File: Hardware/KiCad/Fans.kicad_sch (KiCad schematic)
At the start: 21 parts, among them J7 Conn_01x06, Q1 PSMN8R5-40MSDX, Q5 PSMN8R5-40MSDX

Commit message: revB
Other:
- moved on the sheet: D5, D7, J7, LVPWR16, LVPWR17, LVPWR3, LVPWR6, PWM_A2, PWM_B2, Q1, Q5, R10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

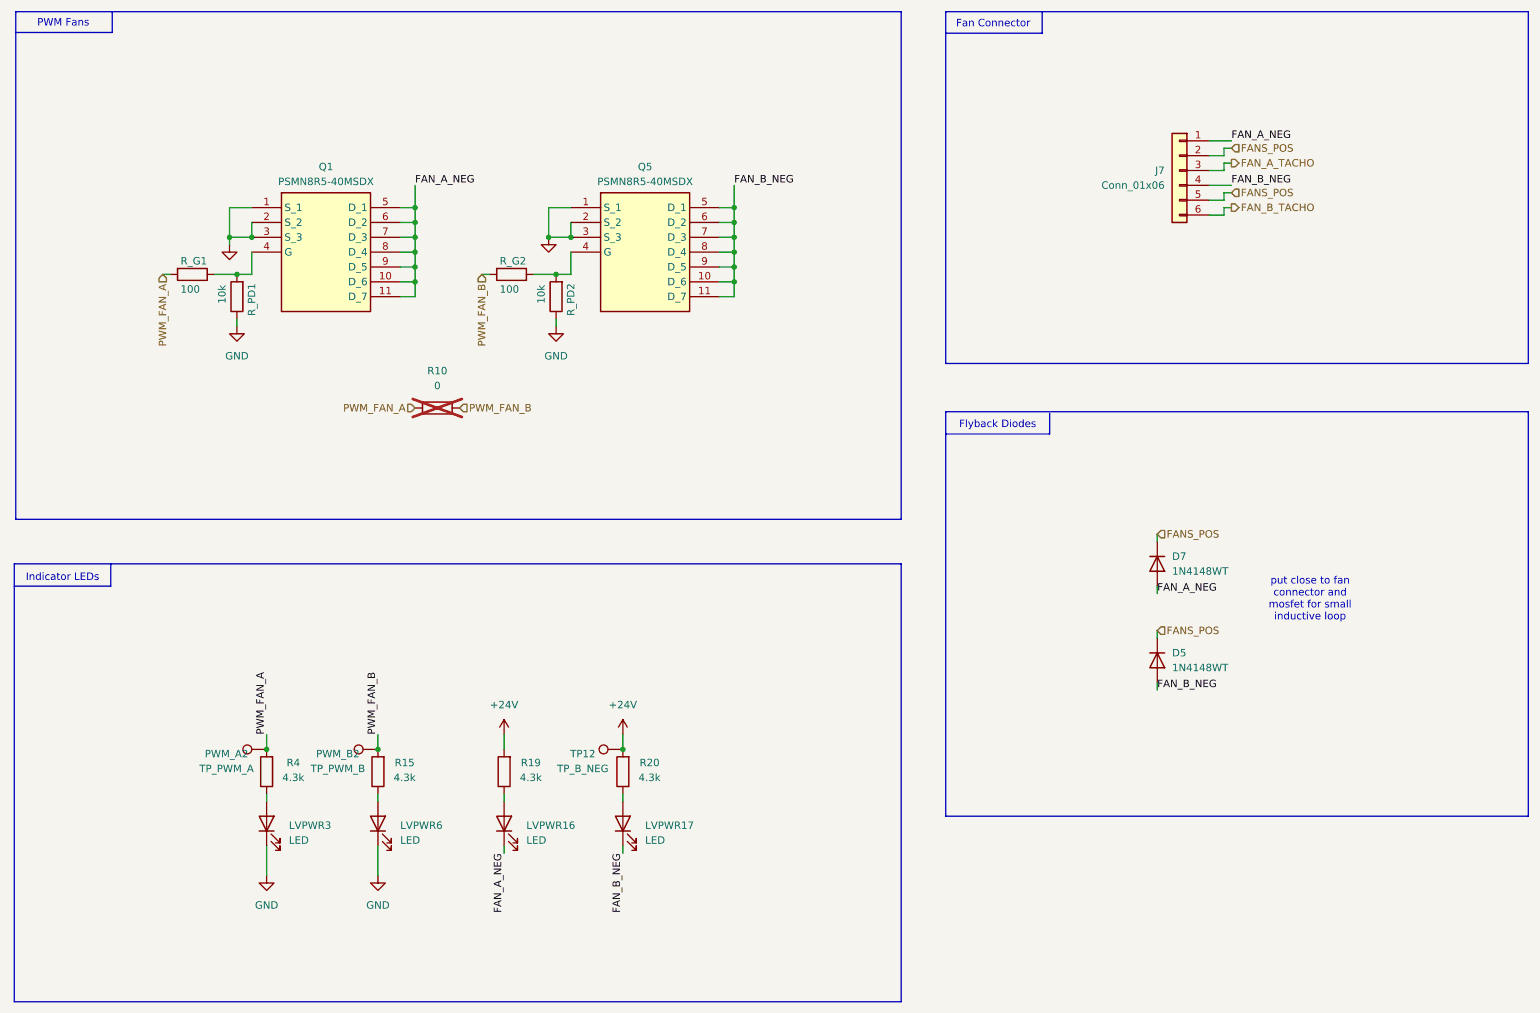
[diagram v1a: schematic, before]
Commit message: schematic changes, pre pcb revB changes
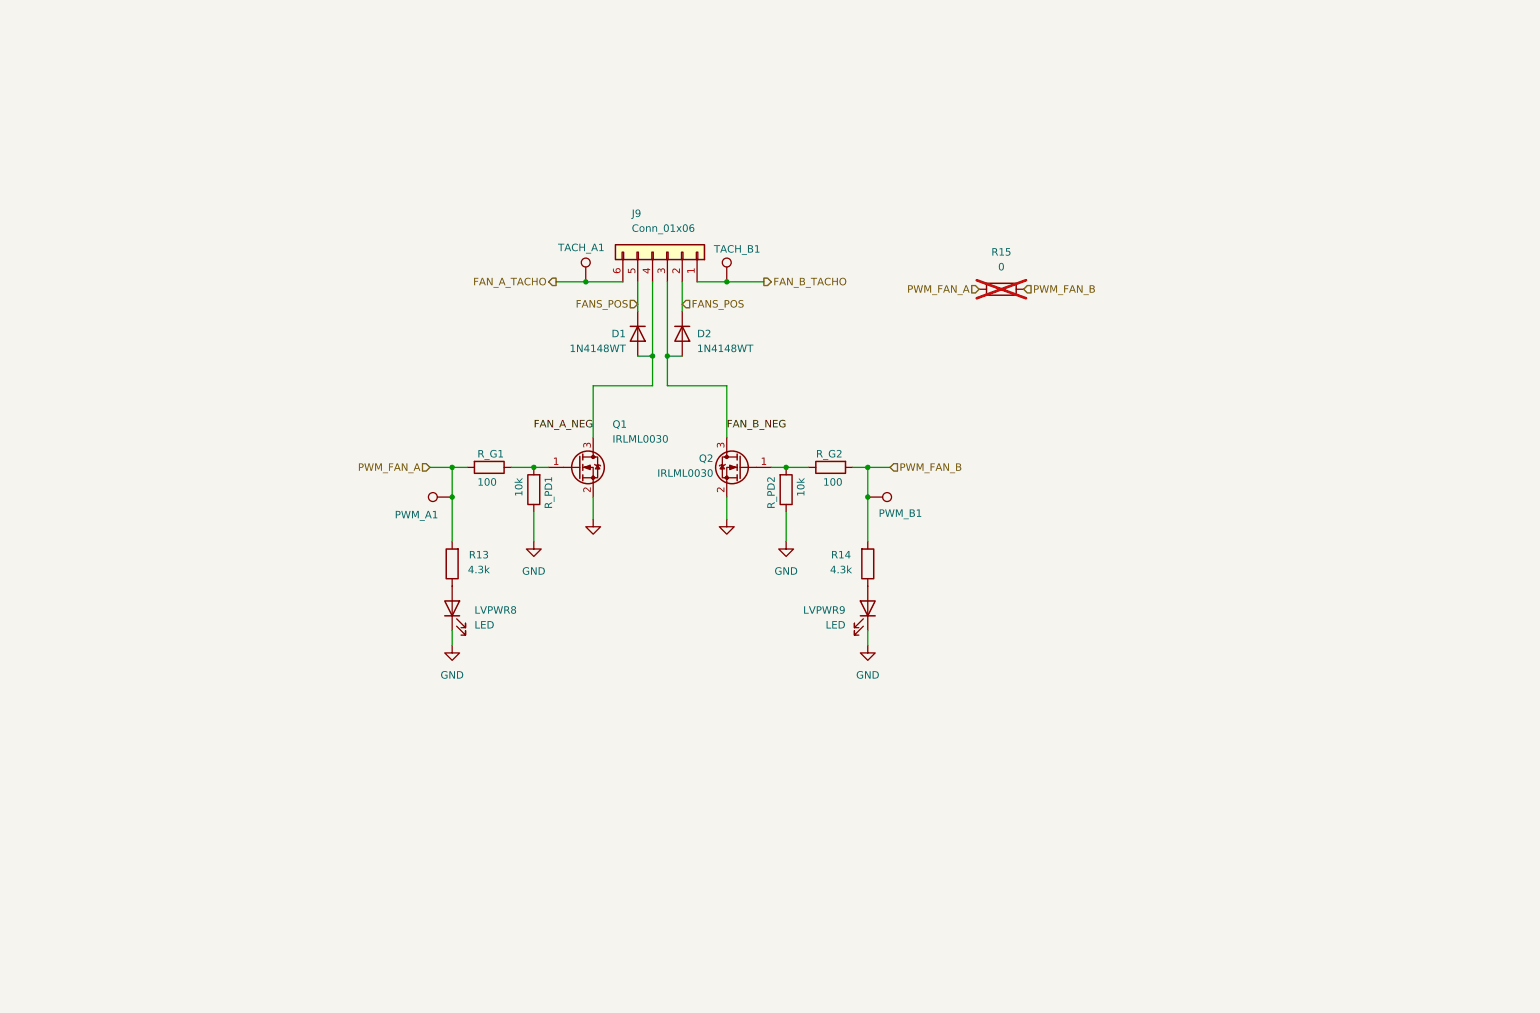
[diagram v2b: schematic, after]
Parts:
- removed LVPWR16, LVPWR17: LED, LED_SMD:LED_0603_1608Metric, symbol Device:LED
- removed Q1, Q5: PSMN8R5-40MSDX, UTSVT_Power:PSMN8R5-40MSDX, symbol UTSVT_Power:PSMN8R5-40MSDX
- removed R19, R20: 4.3k, Resistor_SMD:R_0603_1608Metric_Pad0.98x0.95mm_HandSolder, symbol Device:R
- removed TP12: TP_B_NEG, TestPoint:TestPoint_Pad_1.0x1.0mm, symbol Connector:TestPoint
- added Q1, Q2: IRLML0030, Package_TO_SOT_SMD:SOT-23, symbol Transistor_FET:IRLML0030
- added TACH_A1, TACH_B1: TP_PWM_B, TestPoint:TestPoint_Pad_1.0x1.0mm, symbol Connector:TestPoint
- D1: renamed from D7; footprint Diode_SMD:D_SOD-523 -> easyeda2kicad:SOD-523F_L1.2-W0.8-LS1.7-RD; LCSC (none) -> C27748
- D2: renamed from D5; footprint Diode_SMD:D_SOD-523 -> easyeda2kicad:SOD-523F_L1.2-W0.8-LS1.7-RD; LCSC (none) -> C27748
- R13: renamed from R4; LCSC (none) -> C2907165
- R14: renamed from R15; LCSC (none) -> C2907165
- R15: renamed from R10; LCSC (none) -> C21189
- R_PD1, R_PD2: LCSC (none) -> C25804
- renumbered J7 to J9, LVPWR3 to LVPWR8, LVPWR6 to LVPWR9, PWM_A2 to PWM_A1, PWM_B2 to PWM_B1
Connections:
- net FAN_A_NEG: now also J9.4 (Pin_4), Q1.3 (D); no longer J9.1 (Pin_1)
- net FAN_A_TACHO: now also J9.6 (Pin_6), TACH_A1.1; no longer J9.3 (Pin_3)
- net FAN_B_NEG: now also J9.3 (Pin_3), Q2.3 (D); no longer J9.4 (Pin_4)
- net FAN_B_TACHO: now also J9.1 (Pin_1), TACH_B1.1; no longer J9.6 (Pin_6)
- net GND: now also Q1.2 (S), Q2.2 (S)
- net at R_G2.1, R_PD2.2: now also Q2.1 (G)
- net at R_G1.1, R_PD1.2: now also Q1.1 (G)
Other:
- note removed: "Fan Connector"
- note removed: "Flyback Diodes"
- note removed: "Indicator LEDs"
- note removed: "PWM Fans"
- note removed: "put close to fan connector and mosfet for small inductive loop"
- moved on the sheet: D1, D2, J9, LVPWR8, LVPWR9, PWM_A1, PWM_B1, R13, R14, R15, R_G1, R_PD1

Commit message: revB, will make aesthetic changes
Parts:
- J9: footprint Connector_Molex:Molex_Nano-Fit_105309-xx06_1x06_P2.50mm_Vertical -> Connector_Molex:Molex_Nano-Fit_105313-xx06_1x06_P2.50mm_Horizontal
- renumbered PWM_B1 to PWM_A1, PWM_A1 to PWM_B1, TACH_B1 to TACH_A1, TACH_A1 to TACH_B1
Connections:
- net FAN_A_TACHO: now also J9.1 (Pin_1), TACH_A1.1; no longer J9.6 (Pin_6), TACH_B1.1
- net FAN_B_TACHO: now also J9.6 (Pin_6), TACH_B1.1; no longer J9.1 (Pin_1), TACH_A1.1
- net PWM_FAN_A: now also PWM_A1.1, R14.2, R_G2.2; no longer PWM_B1.1, R13.2, R_G1.2
- net PWM_FAN_B: now also PWM_B1.1, R13.2, R_G1.2; no longer PWM_A1.1, R14.2, R_G2.2
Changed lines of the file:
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@@
 	(wire
 		(pts
-			(xy 139.7 66.04) (xy 146.05 66.04)
+			(xy 139.7 66.04) (xy 144.78 66.04)
 		)
 		(stroke
@@
 	(hierarchical_label "PWM_FAN_B"
 		(shape input)
-		(at 167.64 97.79 0)
+		(at 88.9 97.79 180)
 		(effects
 			(font
 				(size 1.27 1.27)
 			)
-			(justify left)
+			(justify right)
 		)
 	)
 	(hierarchical_label "FAN_A_TACHO"
 		(shape output)
-		(at 110.49 66.04 180)
+		(at 144.78 66.04 0)
 		(effects
 			(font
 				(size 1.27 1.27)
 			)
-			(justify right)
+			(justify left)
 		)
 	)
@@
 	(hierarchical_label "PWM_FAN_A"
 		(shape input)
-		(at 88.9 97.79 180)
+		(at 167.64 97.79 0)
 		(effects
 			(font
 				(size 1.27 1.27)
 			)
-			(justify right)
+			(justify left)
 		)
 	)
 	(hierarchical_label "FAN_B_TACHO"
 		(shape output)
-		(at 146.05 66.04 0)
+		(at 110.49 66.04 180)
 		(effects
 			(font
 				(size 1.27 1.27)
 			)
-			(justify left)
+			(justify right)
 		)
 	)
@@
 		(on_board yes)
 		(dnp no)
-		(property "Reference" "PWM_A1"
+		(property "Reference" "PWM_B1"
 			(at 86.614 105.918 90)
 			(effects
@@
 			(project ""
 				(path "/a2e13c19-ff3a-4e43-a7f5-200fd5b2b978/26b9ca43-4422-48e7-9562-1bb32842f27e"
-					(reference "PWM_A1")
+					(reference "PWM_B1")
 					(unit 1)
 				)
@@
 		(on_board yes)
 		(dnp no)
-		(property "Reference" "TACH_A1"
+		(property "Reference" "TACH_B1"
 			(at 114.808 60.198 0)
 			(effects
@@
 			(project "PS-MotorControllerInterfacePCB"
 				(path "/a2e13c19-ff3a-4e43-a7f5-200fd5b2b978/26b9ca43-4422-48e7-9562-1bb32842f27e"
-					(reference "TACH_A1")
+					(reference "TACH_B1")
 					(unit 1)
 				)
@@
 			)
 		)
-		(property "Footprint" "Connector_Molex:Molex_Nano-Fit_105309-xx06_1x06_P2.50mm_Vertical"
+		(property "Footprint" "Connector_Molex:Molex_Nano-Fit_105313-xx06_1x06_P2.50mm_Horizontal"
 			(at 129.54 60.96 0)
 			(effects
@@
 		(on_board yes)
 		(dnp no)
-		(property "Reference" "PWM_B1"
+		(property "Reference" "PWM_A1"
 			(at 169.418 105.664 90)
 			(effects
@@
 			(project "PS-MotorControllerInterfacePCB"
 				(path "/a2e13c19-ff3a-4e43-a7f5-200fd5b2b978/26b9ca43-4422-48e7-9562-1bb32842f27e"
-					(reference "PWM_B1")
+					(reference "PWM_A1")
 					(unit 1)
 				)
@@
 		(on_board yes)
 		(dnp no)
-		(property "Reference" "TACH_B1"
+		(property "Reference" "TACH_A1"
 			(at 141.478 60.452 0)
 			(effects
@@
 			(project "PS-MotorControllerInterfacePCB"
 				(path "/a2e13c19-ff3a-4e43-a7f5-200fd5b2b978/26b9ca43-4422-48e7-9562-1bb32842f27e"
-					(reference "TACH_B1")
+					(reference "TACH_A1")
 					(unit 1)
 				)

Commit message: revB layout
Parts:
- removed LVPWR8, LVPWR9: LED, LED_SMD:LED_0603_1608Metric, symbol Device:LED
- removed R13, R14: 4.3k, Resistor_SMD:R_0603_1608Metric_Pad0.98x0.95mm_HandSolder, symbol Device:R
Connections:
- net FAN_A_NEG: now also D2.2 (A), Q2.3 (D); no longer D1.2 (A), Q1.3 (D)
- net FAN_B_NEG: now also D1.2 (A), Q1.3 (D); no longer D2.2 (A), Q2.3 (D)
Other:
- moved on the sheet: PWM_A1, PWM_B1

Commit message: sch changes, pre pcb changes
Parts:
- added PD_TACHA1, PD_TACHB1: 10k, Resistor_SMD:R_0603_1608Metric_Pad0.98x0.95mm_HandSolder, symbol Device:R
- D1, D2: footprint easyeda2kicad:SOD-523F_L1.2-W0.8-LS1.7-RD -> Diode_SMD:D_SOD-523
- J9: footprint Connector_Molex:Molex_Nano-Fit_105313-xx06_1x06_P2.50mm_Horizontal -> UTSVT_Connectors:105313-1106
- renumbered R15 to R11
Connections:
- net FAN_A_TACHO: now also PD_TACHA1.1
- net FAN_B_TACHO: now also PD_TACHB1.1
- new net +3V3: PD_TACHA1.2, PD_TACHB1.2
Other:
- moved on the sheet: D1, R11

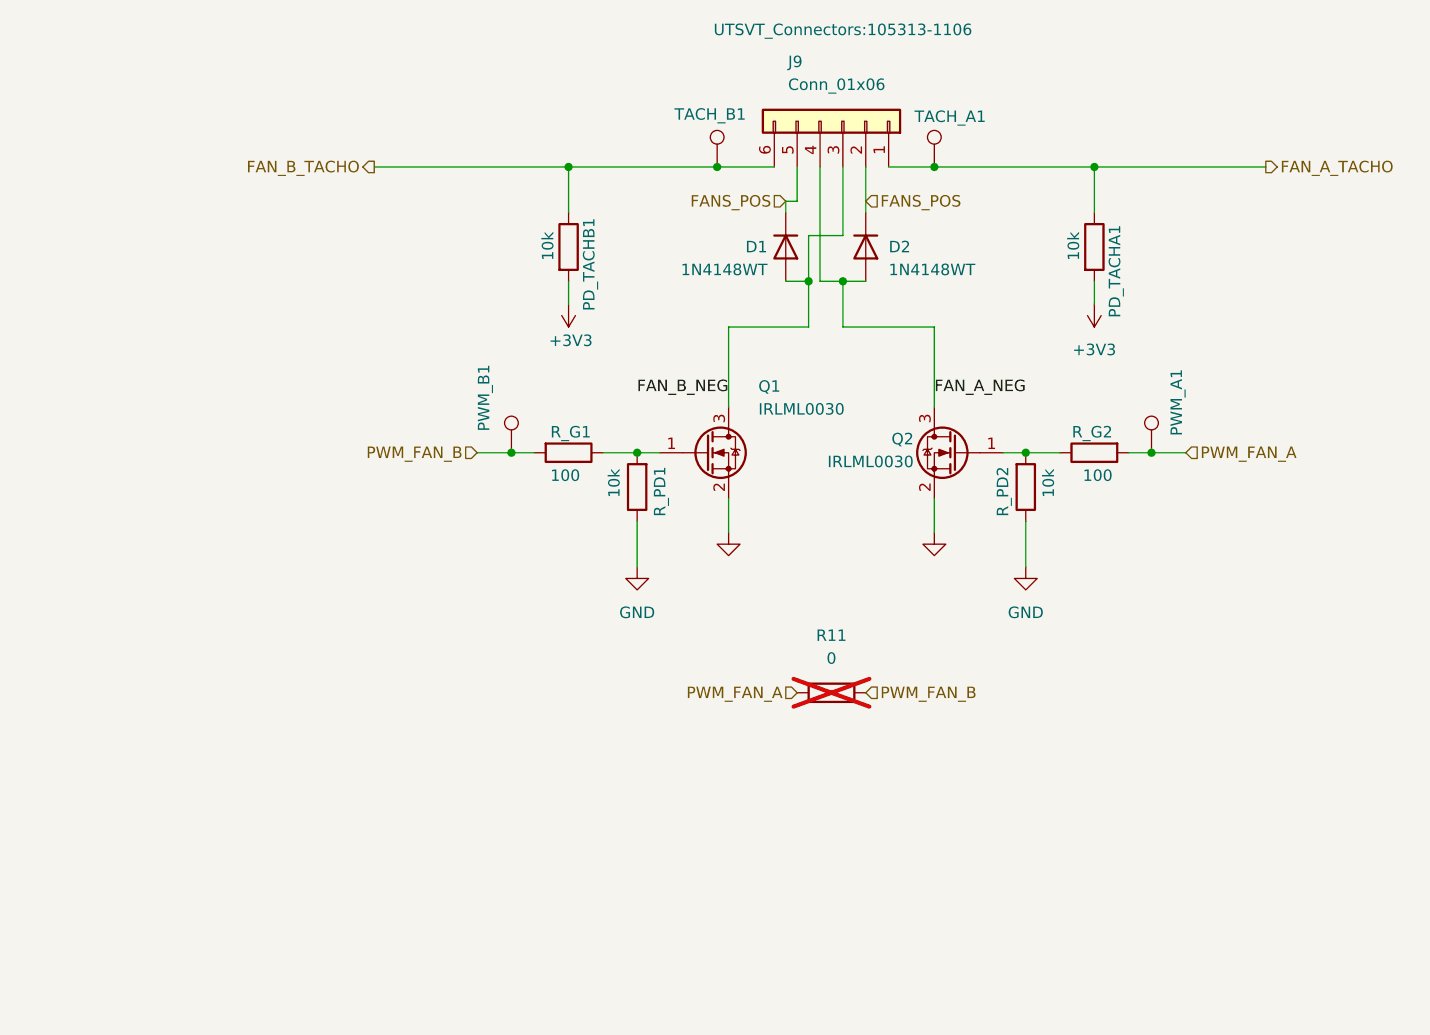
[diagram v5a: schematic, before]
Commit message: layout ready for review
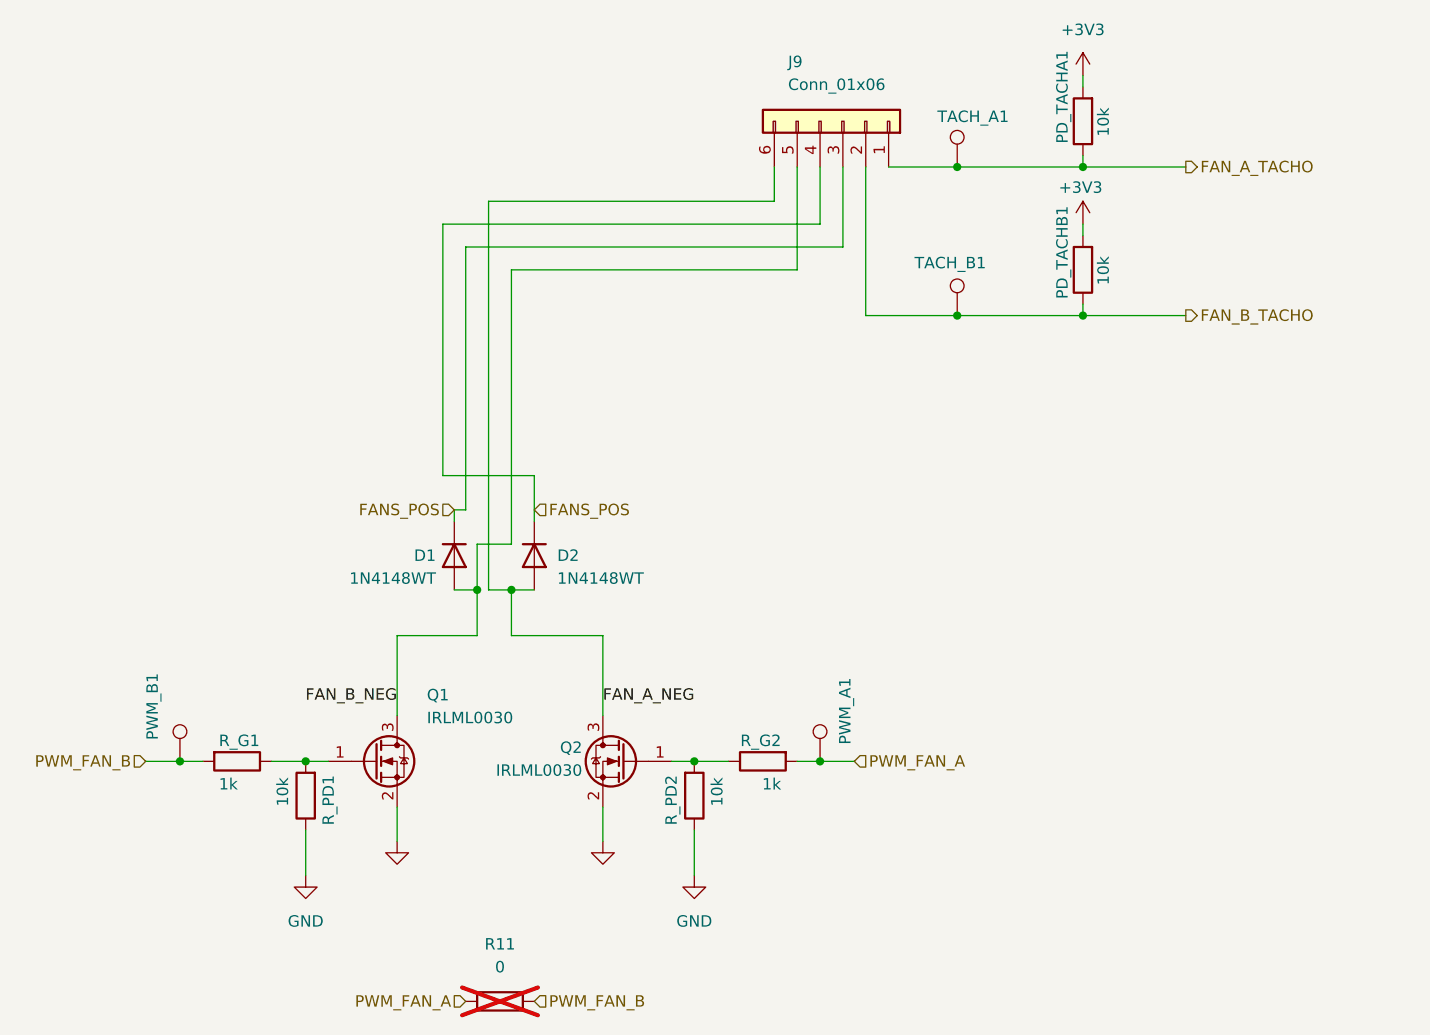
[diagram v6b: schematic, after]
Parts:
- D1, D2: footprint Diode_SMD:D_SOD-523 -> UTSVT_Passives:SODFL4724X108N
- R_G1, R_G2: value 100 -> 1k
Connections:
- net FANS_POS: now also J9.3 (Pin_3), J9.4 (Pin_4); no longer J9.2 (Pin_2), J9.5 (Pin_5)
- net FAN_A_NEG: now also J9.6 (Pin_6); no longer J9.4 (Pin_4)
- net FAN_B_NEG: now also J9.5 (Pin_5); no longer J9.3 (Pin_3)
- net FAN_B_TACHO: now also J9.2 (Pin_2); no longer J9.6 (Pin_6)
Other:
- moved on the sheet: D1, D2, PD_TACHA1, PD_TACHB1, PWM_A1, PWM_B1, Q1, Q2, R11, R_G1, R_G2, R_PD1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

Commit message: layout done
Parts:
- PWM_A1, PWM_B1, TACH_A1, TACH_B1: footprint TestPoint:TestPoint_Pad_1.0x1.0mm -> TestPoint:TestPoint_Pin_1.0x1.0mm
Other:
- moved on the sheet: D1, D2, PD_TACHA1, PD_TACHB1, PWM_A1, PWM_B1, Q1, Q2, R11, R_G1, R_G2, R_PD1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

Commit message: done with changes
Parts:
- PWM_A1, PWM_B1: footprint TestPoint:TestPoint_Pin_1.0x1.0mm -> TestPoint:TestPoint_Keystone_5000-5004_Miniature; now in the parts list
- R_G1, R_G2: value 1k -> 100
- TACH_A1, TACH_B1: footprint TestPoint:TestPoint_Pin_1.0x1.0mm -> TestPoint:TestPoint_Pad_1.0x1.0mm; now in the parts list
- renumbered J9 to FANS1
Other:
- moved on the sheet: D1, D2, FANS1, PD_TACHA1, PD_TACHB1, PWM_A1, PWM_B1, Q1, Q2, R11, R_G1, R_G2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
